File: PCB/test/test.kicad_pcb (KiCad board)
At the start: 2 copper layers, 54.1 x 34.2 mm, 60 parts, among them CN4 HEADER_1X4, CN5 UFL, SW2 MLL1200S_TE, U1 STM32WBxx_QFN48, U2 USBLC6-2SC6, U3 LD3985M33R, X1 NX2016_32MHz, X2 NX2012_32K768Hz

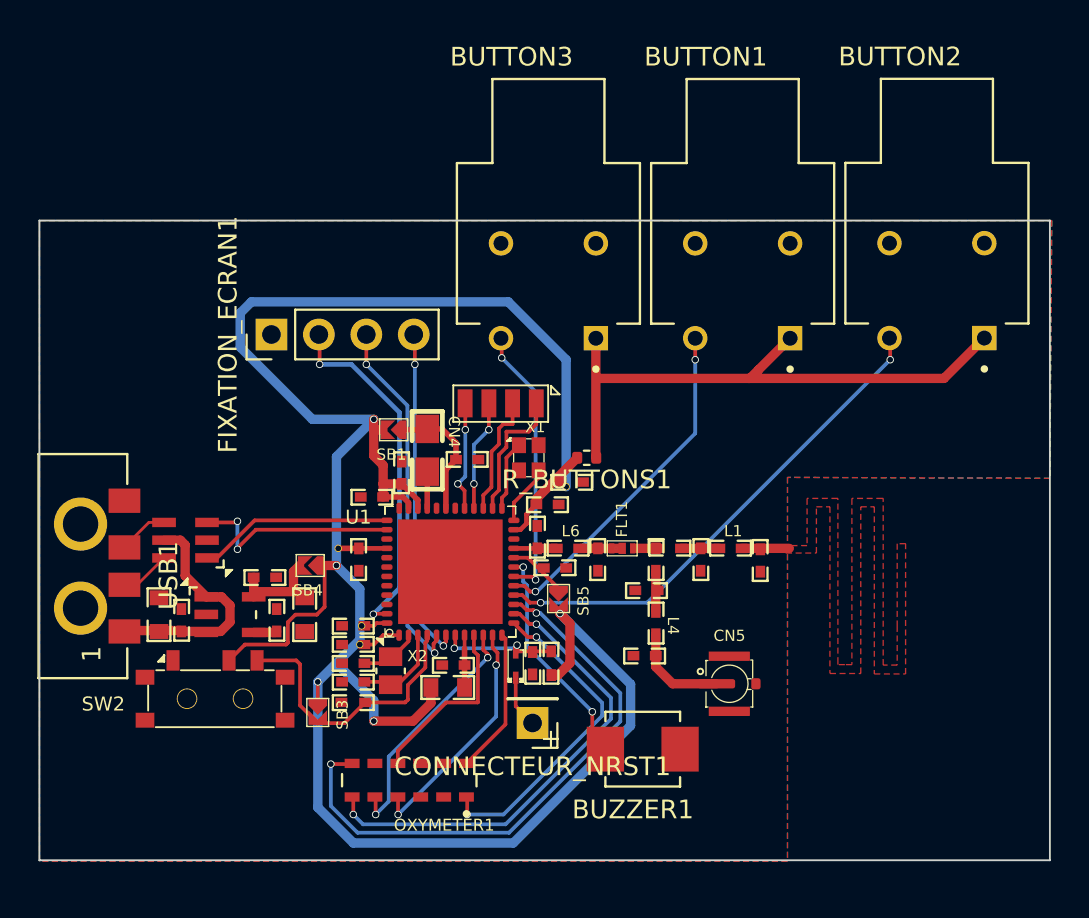
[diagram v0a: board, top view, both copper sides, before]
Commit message: nouveaux boutons, réduction taille
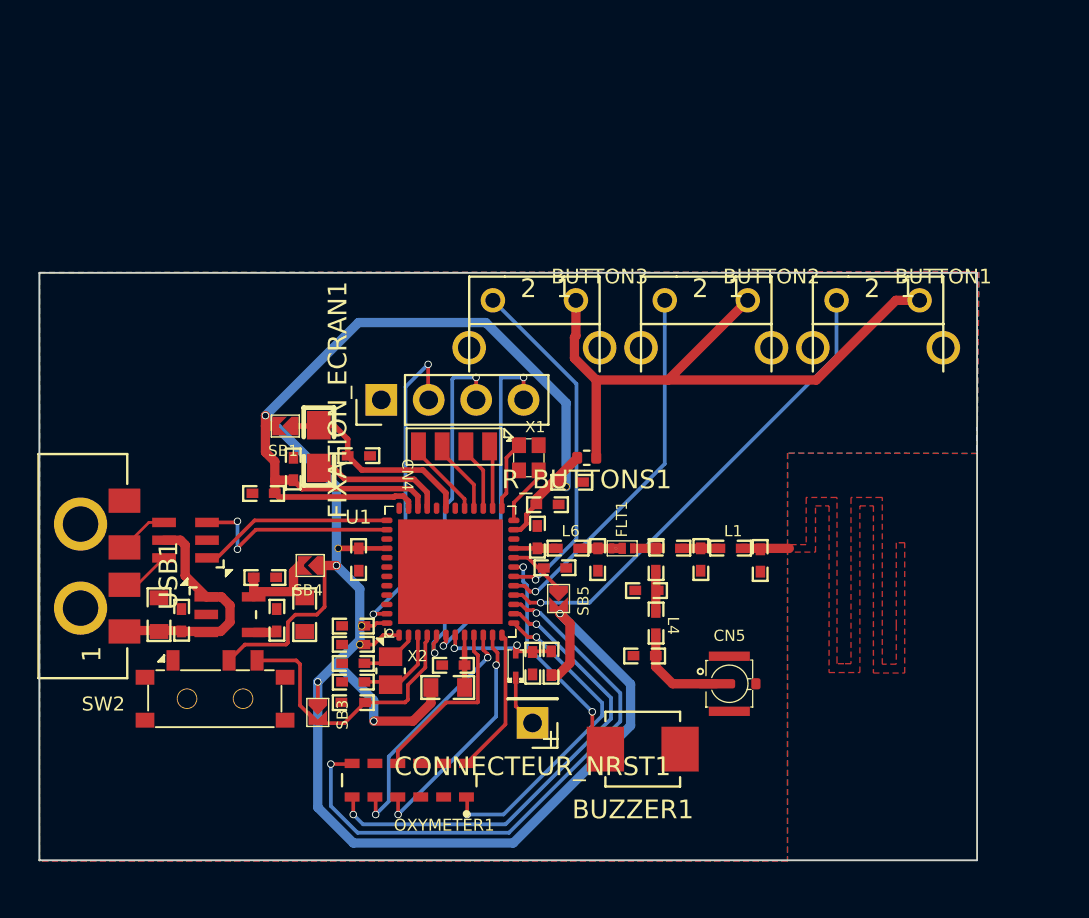
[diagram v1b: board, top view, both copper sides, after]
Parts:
- BUTTON1, BUTTON2, BUTTON3: value MPB02-1B00-R-D -> 9-1437565-9; footprint MPB02-1B00-R-D:SW_MPB02-1B00-R-D -> 9-1437565-9:FSMRACD
- moved BUTTON1 10.8 mm to (161.4, 77.3), turned to 180 degrees
- moved BUTTON2 8.89 mm to (152.2, 77.3), turned to 180 degrees
- moved FIXATION_ECRAN1 6.84 mm to (131.3, 83.9)
- moved C9 5.80 mm to (126.6, 87.6)
- moved SB1 5.80 mm to (126.1, 85.3)
- moved C10 5.80 mm to (130.1, 86.9)
- moved C16 5.80 mm to (125.0, 88.9)
- moved L2 5.80 mm to (128.0, 85.3)
- moved CN4 3.40 mm to (137.1, 86.4)
- moved BUTTON3 2.85 mm to (143.0, 77.3), turned to 180 degrees
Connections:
- R_BUTTONS1 pad 1: Net-(BUTTON1-Pad1) -> Net-(BUTTON1-PadP$1)
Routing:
- net Net-(BUTTON1-PadP$1): track 0.00 -> 34.1 mm
- net Net-(BUTTON1-Pad1): track 31.0 -> 0.00 mm
- net Net-(L2-Pad2): track 1.96 -> 7.19 mm
- net Net-(C10-Pad1): track 6.95 -> 11.0 mm
- net PA9: track 15.0 -> 19.0 mm, vias 2 -> 1
- net Net-(CN4-Pad1): track 7.29 -> 3.38 mm
- net Net-(CN4-Pad2): track 6.55 -> 3.70 mm
- net PB0: track 5.95 -> 4.02 mm, vias 2 -> 0
- net Net-(FIXATION_ECRAN1-Pad2): track 19.1 -> 17.2 mm
- net PB1: track 5.93 -> 4.34 mm, vias 2 -> 0
- net PA8: track 18.4 -> 19.9 mm, vias 2 -> 1
- net 3V3: track 131.6 -> 132.6 mm
- net Net-(FIXATION_ECRAN1-Pad3): track 19.6 -> 18.7 mm
- net PA7: track 26.8 -> 25.9 mm, vias 2 -> 1
- net Net-(FIXATION_ECRAN1-Pad4): track 18.0 -> 18.7 mm
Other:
- board size 54.1 x 34.2 mm -> 50.2 x 31.5 mm

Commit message: correction d'erreurs + compacité
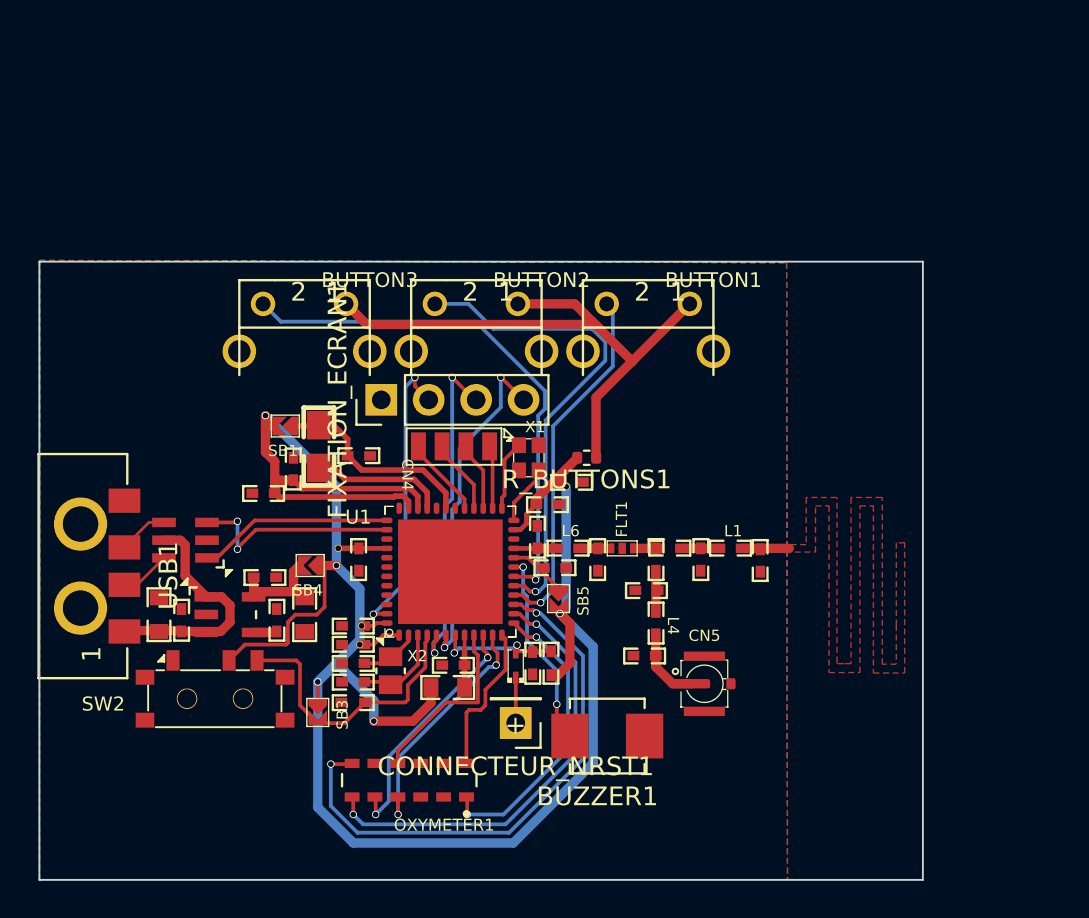
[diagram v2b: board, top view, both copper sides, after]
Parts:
- moved BUTTON1 12.3 mm to (149.1, 77.5)
- moved BUTTON2 12.3 mm to (139.9, 77.5)
- moved BUTTON3 12.3 mm to (130.7, 77.5)
- moved BUZZER1 2.02 mm to (143.4, 101.9)
- moved CN5 1.34 mm to (148.6, 99.1)
- moved CONNECTEUR_NRST1 0.90 mm to (138.5, 101.2)
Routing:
- net 3V3: track 132.6 -> 113.4 mm
- net PA9: track 19.0 -> 28.6 mm
- net PA7: track 25.9 -> 19.3 mm
- net PA8: track 19.9 -> 26.3 mm
- net Net-(BUTTON1-PadP$1): track 34.1 -> 31.8 mm
- net PA6: track 31.1 -> 29.5 mm
- net PA5: track 25.5 -> 23.9 mm
- net PA4: track 17.6 -> 16.0 mm
- net PB2: track 12.1 -> 10.6 mm
- net Net-(FIXATION_ECRAN1-Pad2): track 17.2 -> 15.8 mm
- net Net-(C29-Pad1): track 5.37 -> 4.04 mm
- net Net-(FIXATION_ECRAN1-Pad3): track 18.7 -> 18.0 mm
- net Net-(FIXATION_ECRAN1-Pad4): track 18.7 -> 18.1 mm
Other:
- board size 50.2 x 31.5 mm -> 47.3 x 33.1 mm

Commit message: fix d'une erreur
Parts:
- removed C1: 100nF, Library:0402_CAP_NPOL
- removed C2: 100pF, Library:0402_CAP_NPOL
- moved R_BUTTONS1 1.10 mm to (141.2, 86.9), turned to -90 degrees
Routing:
- net 3V3: track 113.4 -> 109.1 mm

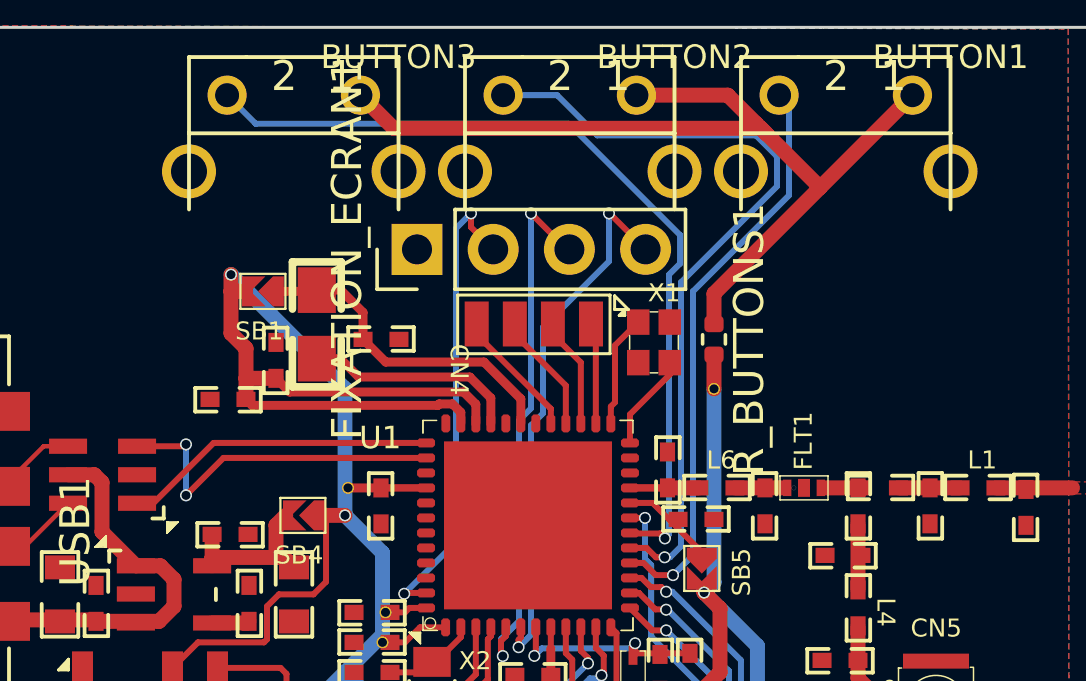
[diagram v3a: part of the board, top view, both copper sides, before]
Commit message: Revert "fix d'une erreur"
This reverts commit d237dfa0d90c399318c3ec0f34094da9eb165235.
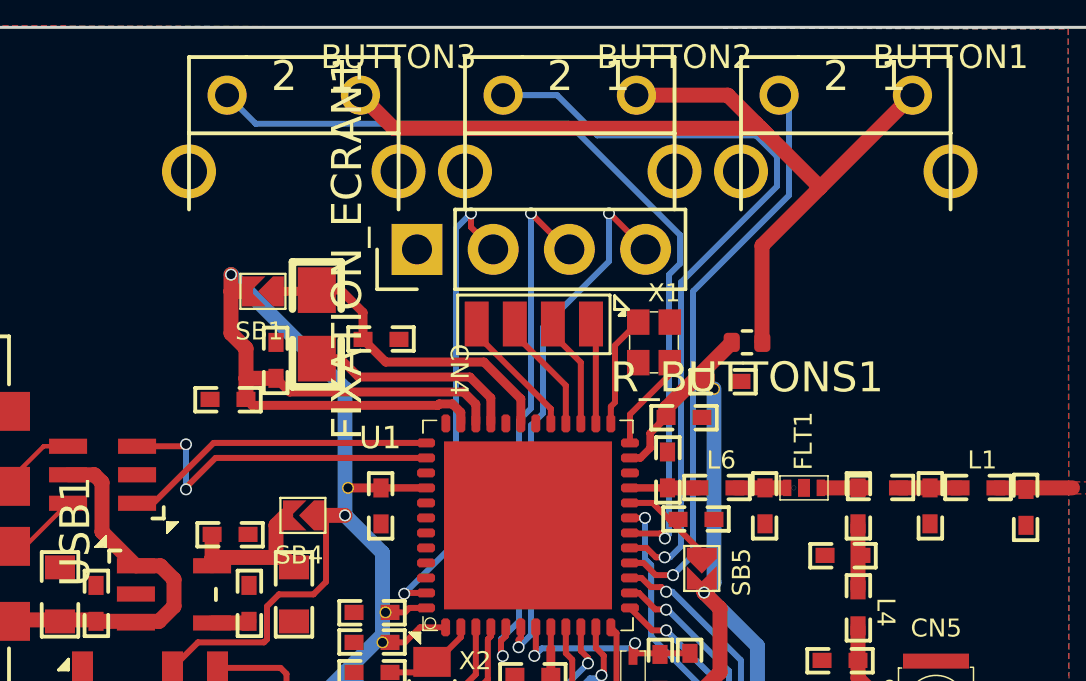
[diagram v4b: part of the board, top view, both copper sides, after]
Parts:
- added C1: 100nF, Library:0402_CAP_NPOL, F.Cu at (140.2, 89.5)
- added C2: 100pF, Library:0402_CAP_NPOL, F.Cu at (141.5, 88.3)
- moved R_BUTTONS1 1.10 mm to (142.3, 87.0), turned to 180 degrees
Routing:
- net 3V3: track 109.1 -> 113.4 mm

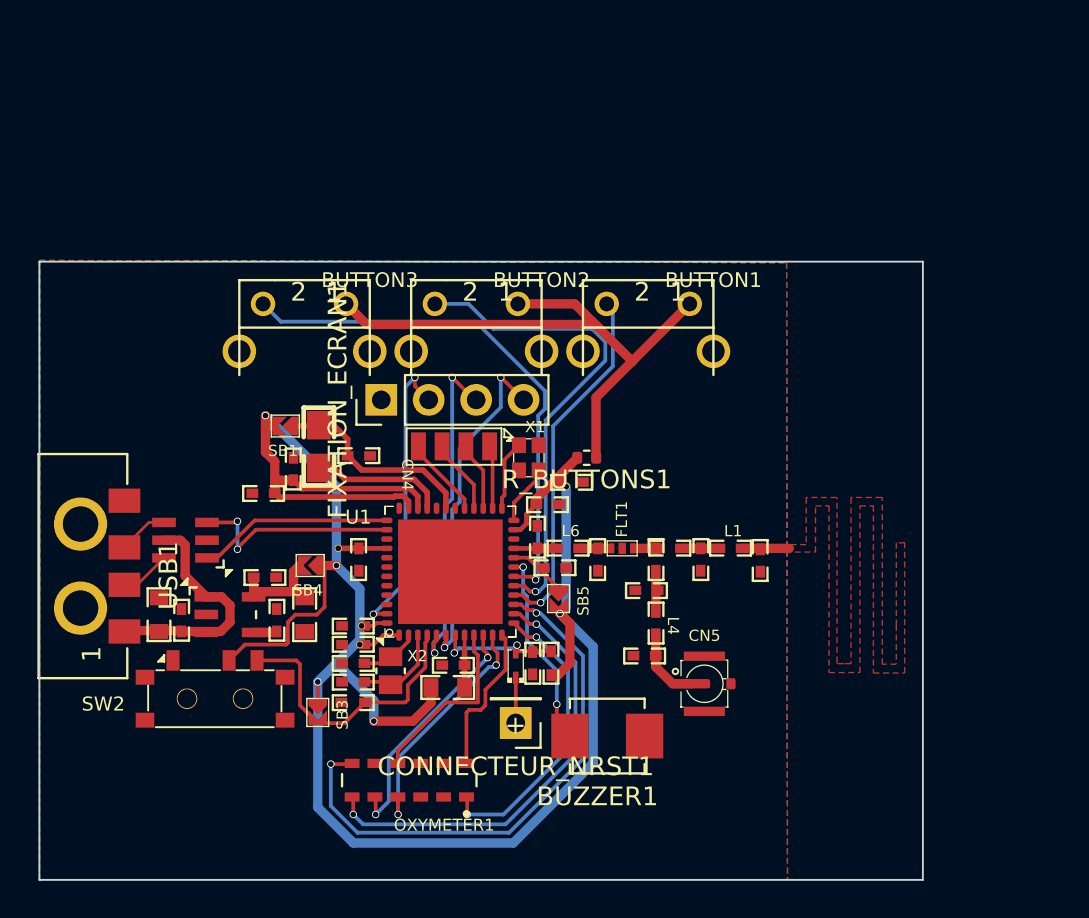
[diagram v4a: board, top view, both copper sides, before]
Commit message: réduction taille des routes
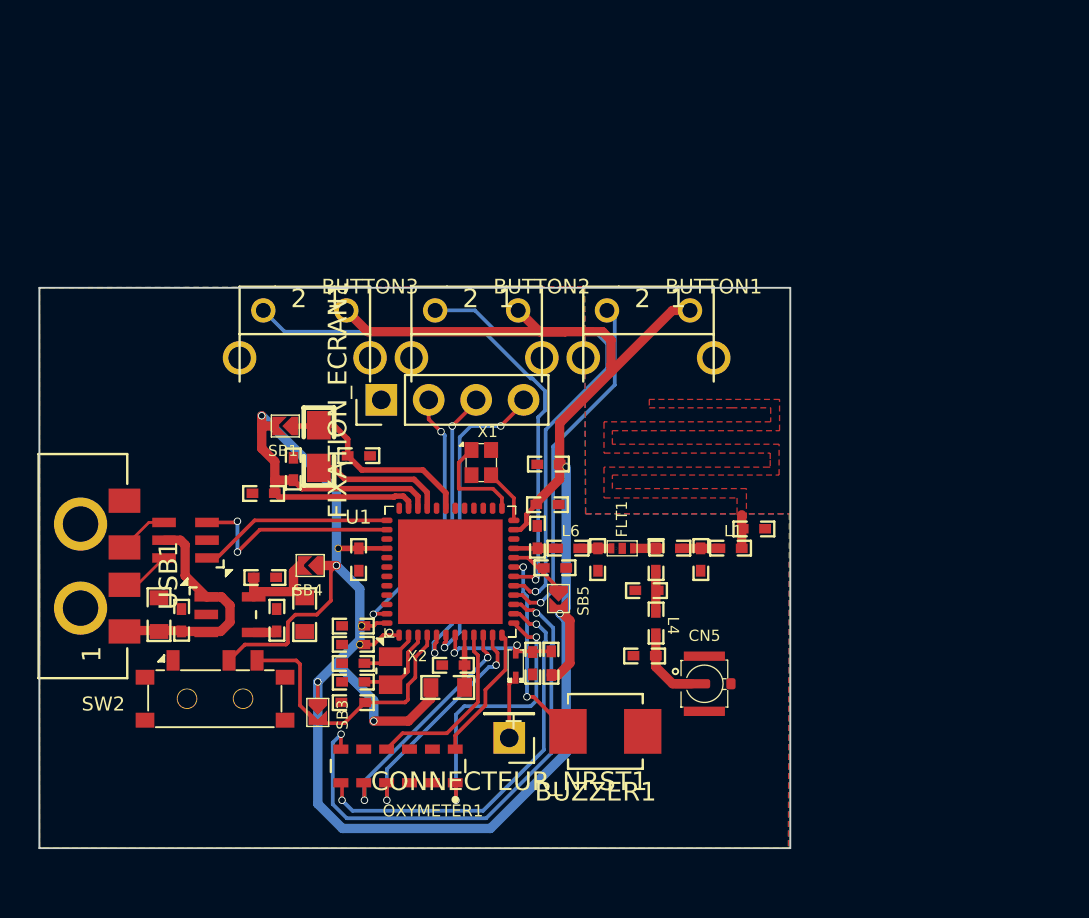
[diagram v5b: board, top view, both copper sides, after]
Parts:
- removed CN4: HEADER_1X4, Library:SIL4_127_B
- removed R_BUTTONS1: 330, Resistor_SMD:R_0402_1005Metric
- moved X1 2.56 mm to (136.7, 87.3)
- moved C7 1.74 mm to (151.2, 90.8), turned to 180 degrees
- moved C2 1.57 mm to (140.2, 87.3), turned to 0 degrees
- moved ? 1.05 mm to (141.2, 87.5)
- moved OXYMETER1 0.97 mm to (132.2, 103.5)
- moved CONNECTEUR_NRST1 0.87 mm to (138.2, 102.0)
- moved BUTTON2 0.35 mm to (139.9, 77.8)
- moved BUTTON1 0.35 mm to (149.1, 77.8)
- moved BUTTON3 0.35 mm to (130.7, 77.8)
- moved BUZZER1 0.27 mm to (143.3, 101.7)
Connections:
- BUTTON1 pad P$1: Net-(BUTTON1-PadP$1) -> 3V3
- BUTTON2 pad P$1: Net-(BUTTON1-PadP$1) -> 3V3
- BUTTON3 pad GND2: GND -> unconnected-(BUTTON3-PadGND2)
- BUTTON3 pad P$1: Net-(BUTTON1-PadP$1) -> 3V3
- U1 pad 26: Net-(CN4-Pad1) -> unconnected-(U1-Pad26)
- U1 pad 27: Net-(CN4-Pad2) -> unconnected-(U1-Pad27)
- U1 pad 28: PB0 -> unconnected-(U1-Pad28)
- U1 pad 29: PB1 -> unconnected-(U1-Pad29)
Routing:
- net Net-(BUTTON1-PadP$1): track 31.8 -> 0.00 mm
- net 3V3: track 113.4 -> 142.6 mm
- net PB1: track 4.34 -> 0.00 mm
- net PB0: track 4.02 -> 0.00 mm
- net Net-(CN4-Pad2): track 3.70 -> 0.00 mm
- net Net-(CN4-Pad1): track 3.38 -> 0.00 mm
- net Net-(FIXATION_ECRAN1-Pad3): track 18.0 -> 15.5 mm
- net PA5: track 23.9 -> 21.8 mm
- net PA6: track 29.5 -> 27.6 mm
- net Net-(FIXATION_ECRAN1-Pad2): track 15.8 -> 14.2 mm
- net Net-(U1-Pad25): track 3.76 -> 5.43 mm
- net Net-(FIXATION_ECRAN1-Pad4): track 18.1 -> 16.6 mm
- net PA4: track 16.0 -> 15.1 mm
- net NRST: track 2.42 -> 3.37 mm
- net PA3: track 8.17 -> 7.29 mm
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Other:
- board size 47.3 x 33.1 mm -> 40.2 x 30 mm
